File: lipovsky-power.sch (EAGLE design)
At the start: 103 parts, among them J1 M04-929J, J2 M04-929J, J3 M04-929J, J4 M04-929J, Q1 NMOS30V_30A, Q11 NMOS40V_10A, Q12 NMOS40V_10A, Q14 NMOS40V_10A, Q15 NMOS40V_10A, Q16 NMOS40V_10A, Q18 NMOS40V_10A, Q2 2NMOS30V_0.1A, Q21 PMOS30V_11A, Q22 PMOS30V_11A, Q23 NMOS40V_10A, Q24 NMOS40V_10A, Q25 PMOS30V_11A, Q26 PMOS30V_11A, Q27 NMOS40V_10A, Q28 NMOS40V_10A, Q3 2PMOS50V_0.17A, Q31 PMOS30V_11A, Q32 PMOS30V_11A, Q33 PMOS30V_11A, Q34 PMOS30V_11A, Q35 PMOS30V_11A, Q36 PMOS30V_11A, Q37 PMOS30V_11A, Q38 PMOS30V_11A, Q4 2PMOS50V_0.17A, Q41 PMOS30V_11A, Q42 PMOS30V_11A, Q43 PMOS30V_11A, Q44 PMOS30V_11A, Q45 PMOS30V_11A, Q46 PMOS30V_11A, Q47 PMOS30V_11A, Q48 PMOS30V_11A, Q5 2NMOS30V_0.1A, Q51 PMOS30V_11A, Q52 PMOS30V_11A, Q53 PMOS30V_11A, Q54 PMOS30V_11A, Q55 PMOS30V_11A, Q56 PMOS30V_11A, Q57 PMOS30V_11A, Q58 PMOS30V_11A, Q62 PMOS30V_11A, Q64 PMOS30V_11A, Q66 PMOS30V_11A, Q68 PMOS30V_11A, T1 TFORM_4_4311_4A4, U1 DG508BEN-T1-GE4, U2 DG508BEN-T1-GE4, U3 74HC595, U4 LTC3805-5IDD, U5 TC1240A, U6 AR30N60PPA-13

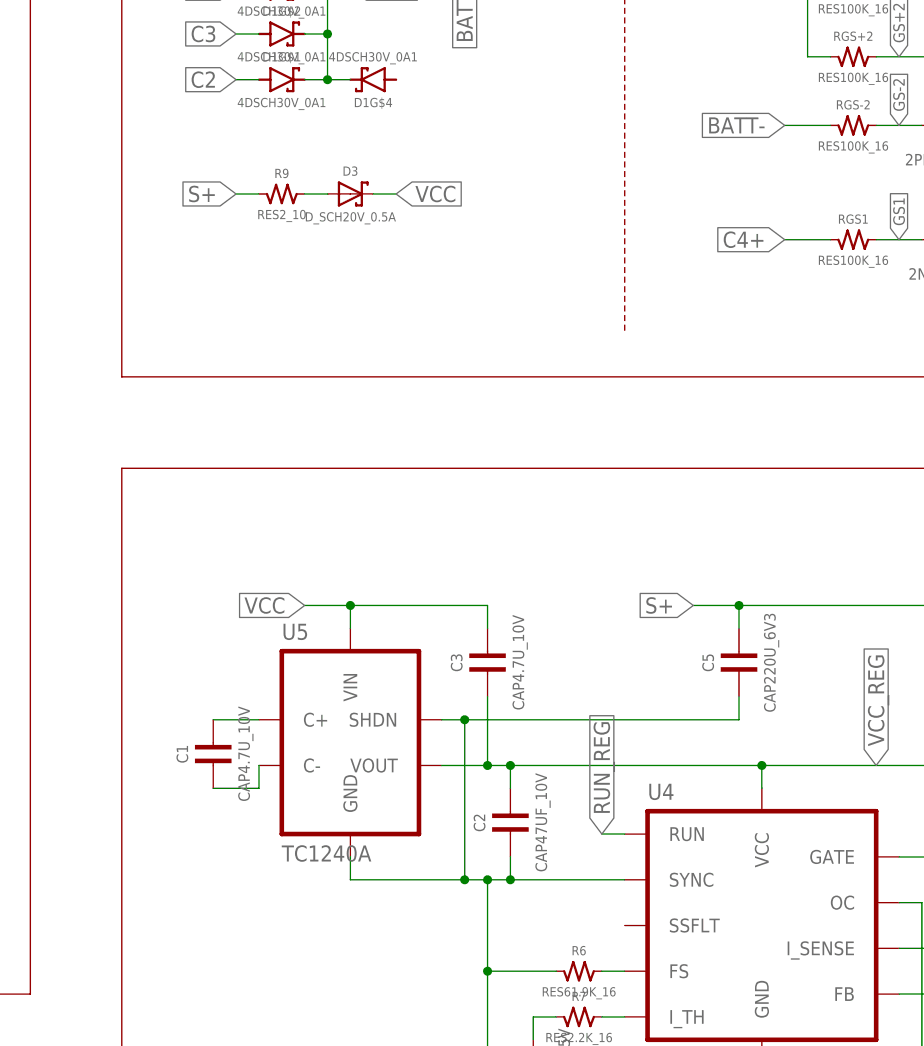
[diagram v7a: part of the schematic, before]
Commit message: moving boosters
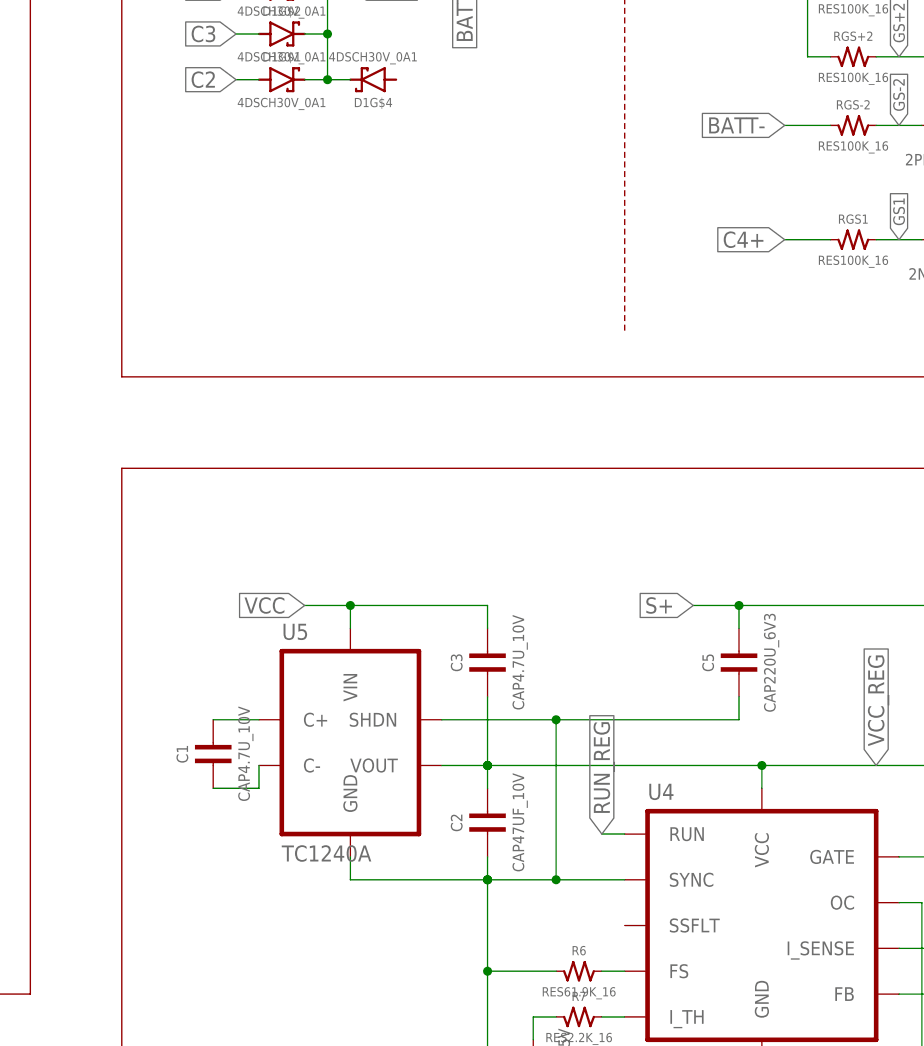
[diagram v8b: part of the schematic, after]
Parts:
- removed D3: D_SCH20V_0.5A, dubec:D_SCH20V_0.5A
- removed R9: RES2_10, dubec:RES2_10
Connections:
- removed net N$11: D3.A, R9.2
- net S+: no longer R9.1
- net VCC: no longer D3.C
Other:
- moved on the sheet: C2
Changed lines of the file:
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@@
 <part name="U4" library="dubec" deviceset="LTC3805-5" device="IDD"/>
 <part name="R8" library="dubec" deviceset="RES" device="15.4K_16"/>
-<part name="R9" library="dubec" deviceset="RES" device="2_10"/>
-<part name="D3" library="dubec" deviceset="D_SCH" device="20V_0.5A"/>
 <part name="R10" library="dubec" deviceset="RES" device="100K_16"/>
 <part name="C3" library="dubec" deviceset="CAP" device="4.7U_10V" value="CAP4.7U_10V"/>
@@
 <instance part="R7" gate="G$1" x="55.88" y="-66.04"/>
 <instance part="C4" gate="G$1" x="50.8" y="-73.66" rot="R90"/>
-<instance part="C2" gate="G$1" x="48.26" y="-45.72" rot="R90"/>
+<instance part="C2" gate="G$1" x="45.72" y="-45.72" rot="R90"/>
 <instance part="C1" gate="G$1" x="15.24" y="-38.1" rot="R90"/>
 <instance part="C5" gate="G$1" x="73.66" y="-27.94" rot="R90"/>
 <instance part="U4" gate="G$1" x="76.2" y="-55.88"/>
 <instance part="R8" gate="G$1" x="99.06" y="-58.42"/>
-<instance part="R9" gate="G$1" x="22.86" y="25.4"/>
-<instance part="D3" gate="G$1" x="30.48" y="25.4"/>
 <instance part="R10" gate="G$1" x="116.84" y="22.86" rot="R90"/>
 <instance part="C3" gate="G$1" x="45.72" y="-27.94" rot="R90"/>
@@
 <pinref part="U5" gate="G$1" pin="GND"/>
 <wire x1="30.48" y1="-48.26" x2="30.48" y2="-50.8" width="0.1524" layer="91"/>
-<wire x1="30.48" y1="-50.8" x2="43.18" y2="-50.8" width="0.1524" layer="91"/>
+<wire x1="30.48" y1="-50.8" x2="45.72" y2="-50.8" width="0.1524" layer="91"/>
 <pinref part="U5" gate="G$1" pin="SHDN"/>
 <pinref part="C5" gate="G$1" pin="1"/>
 <wire x1="73.66" y1="-30.48" x2="73.66" y2="-33.02" width="0.1524" layer="91"/>
-<wire x1="73.66" y1="-33.02" x2="43.18" y2="-33.02" width="0.1524" layer="91"/>
-<wire x1="43.18" y1="-33.02" x2="40.64" y2="-33.02" width="0.1524" layer="91"/>
+<wire x1="73.66" y1="-33.02" x2="53.34" y2="-33.02" width="0.1524" layer="91"/>
+<wire x1="53.34" y1="-33.02" x2="40.64" y2="-33.02" width="0.1524" layer="91"/>
 <label x="76.2" y="-81.28" size="1.778" layer="95" rot="R270" xref="yes"/>
 <pinref part="C2" gate="G$1" pin="1"/>
@@
 <junction x="45.72" y="-60.96"/>
 <pinref part="U4" gate="G$1" pin="SYNC"/>
-<wire x1="60.96" y1="-50.8" x2="48.26" y2="-50.8" width="0.1524" layer="91"/>
-<wire x1="48.26" y1="-50.8" x2="45.72" y2="-50.8" width="0.1524" layer="91"/>
-<wire x1="48.26" y1="-48.26" x2="48.26" y2="-50.8" width="0.1524" layer="91"/>
-<junction x="48.26" y="-50.8"/>
+<wire x1="60.96" y1="-50.8" x2="53.34" y2="-50.8" width="0.1524" layer="91"/>
+<wire x1="53.34" y1="-50.8" x2="45.72" y2="-50.8" width="0.1524" layer="91"/>
+<wire x1="45.72" y1="-48.26" x2="45.72" y2="-50.8" width="0.1524" layer="91"/>
+<junction x="45.72" y="-50.8"/>
 <pinref part="R5" gate="G$1" pin="1"/>
 <wire x1="104.14" y1="-71.12" x2="104.14" y2="-78.74" width="0.1524" layer="91"/>
@@
 <wire x1="76.2" y1="-78.74" x2="76.2" y2="-71.12" width="0.1524" layer="91"/>
 <junction x="45.72" y="-50.8"/>
-<wire x1="43.18" y1="-50.8" x2="45.72" y2="-50.8" width="0.1524" layer="91"/>
 <wire x1="104.14" y1="-78.74" x2="119.38" y2="-78.74" width="0.1524" layer="91"/>
 <junction x="104.14" y="-78.74"/>
 <pinref part="Q5" gate="G$1" pin="S"/>
 <wire x1="119.38" y1="-78.74" x2="119.38" y2="-60.96" width="0.1524" layer="91"/>
-<wire x1="43.18" y1="-33.02" x2="43.18" y2="-50.8" width="0.1524" layer="91"/>
-<junction x="43.18" y="-33.02"/>
-<junction x="43.18" y="-50.8"/>
 <wire x1="76.2" y1="-78.74" x2="76.2" y2="-81.28" width="0.1524" layer="91"/>
+<wire x1="53.34" y1="-33.02" x2="53.34" y2="-50.8" width="0.1524" layer="91"/>
+<junction x="53.34" y="-33.02"/>
+<junction x="53.34" y="-50.8"/>
 </segment>
 <segment>
@@
 <wire x1="73.66" y1="-20.32" x2="68.58" y2="-20.32" width="0.1524" layer="91"/>
 <junction x="73.66" y="-20.32"/>
-</segment>
-<segment>
-<wire x1="20.32" y1="25.4" x2="17.78" y2="25.4" width="0.1524" layer="91"/>
-<label x="17.78" y="25.4" size="1.778" layer="95" rot="R180" xref="yes"/>
-<pinref part="R9" gate="G$1" pin="1"/>
 </segment>
 <segment>
@@
 <net name="VCC" class="0">
 <segment>
-<label x="35.56" y="25.4" size="1.778" layer="95" xref="yes"/>
-<wire x1="33.02" y1="25.4" x2="35.56" y2="25.4" width="0.1524" layer="91"/>
-<pinref part="D3" gate="G$1" pin="C"/>
-</segment>
-<segment>
 <pinref part="U3" gate="G$1" pin="VCC"/>
 <wire x1="269.24" y1="71.12" x2="269.24" y2="76.2" width="0.1524" layer="91"/>
@@
 <pinref part="U5" gate="G$1" pin="VOUT"/>
 <wire x1="40.64" y1="-38.1" x2="45.72" y2="-38.1" width="0.1524" layer="91"/>
-<wire x1="45.72" y1="-38.1" x2="48.26" y2="-38.1" width="0.1524" layer="91"/>
-<wire x1="48.26" y1="-38.1" x2="76.2" y2="-38.1" width="0.1524" layer="91"/>
+<wire x1="45.72" y1="-38.1" x2="76.2" y2="-38.1" width="0.1524" layer="91"/>
 <wire x1="76.2" y1="-38.1" x2="76.2" y2="-40.64" width="0.1524" layer="91"/>
 <junction x="45.72" y="-38.1"/>
@@
 <wire x1="76.2" y1="-38.1" x2="119.38" y2="-38.1" width="0.1524" layer="91"/>
 <wire x1="119.38" y1="-38.1" x2="119.38" y2="-40.64" width="0.1524" layer="91"/>
-<wire x1="48.26" y1="-38.1" x2="48.26" y2="-40.64" width="0.1524" layer="91"/>
-<junction x="48.26" y="-38.1"/>
+<wire x1="45.72" y1="-38.1" x2="45.72" y2="-40.64" width="0.1524" layer="91"/>
+<junction x="45.72" y="-38.1"/>
 <label x="88.9" y="-38.1" size="1.778" layer="95" rot="R90" xref="yes"/>
 </segment>
@@
 </segment>
 </net>
-<net name="N$11" class="0">
-<segment>
-<pinref part="R9" gate="G$1" pin="2"/>
-<pinref part="D3" gate="G$1" pin="A"/>
-<wire x1="25.4" y1="25.4" x2="27.94" y2="25.4" width="0.1524" layer="91"/>
-</segment>
-</net>
